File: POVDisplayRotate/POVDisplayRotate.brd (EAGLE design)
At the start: 80 x 99 mm, 34 parts, among them IC1 317EMP

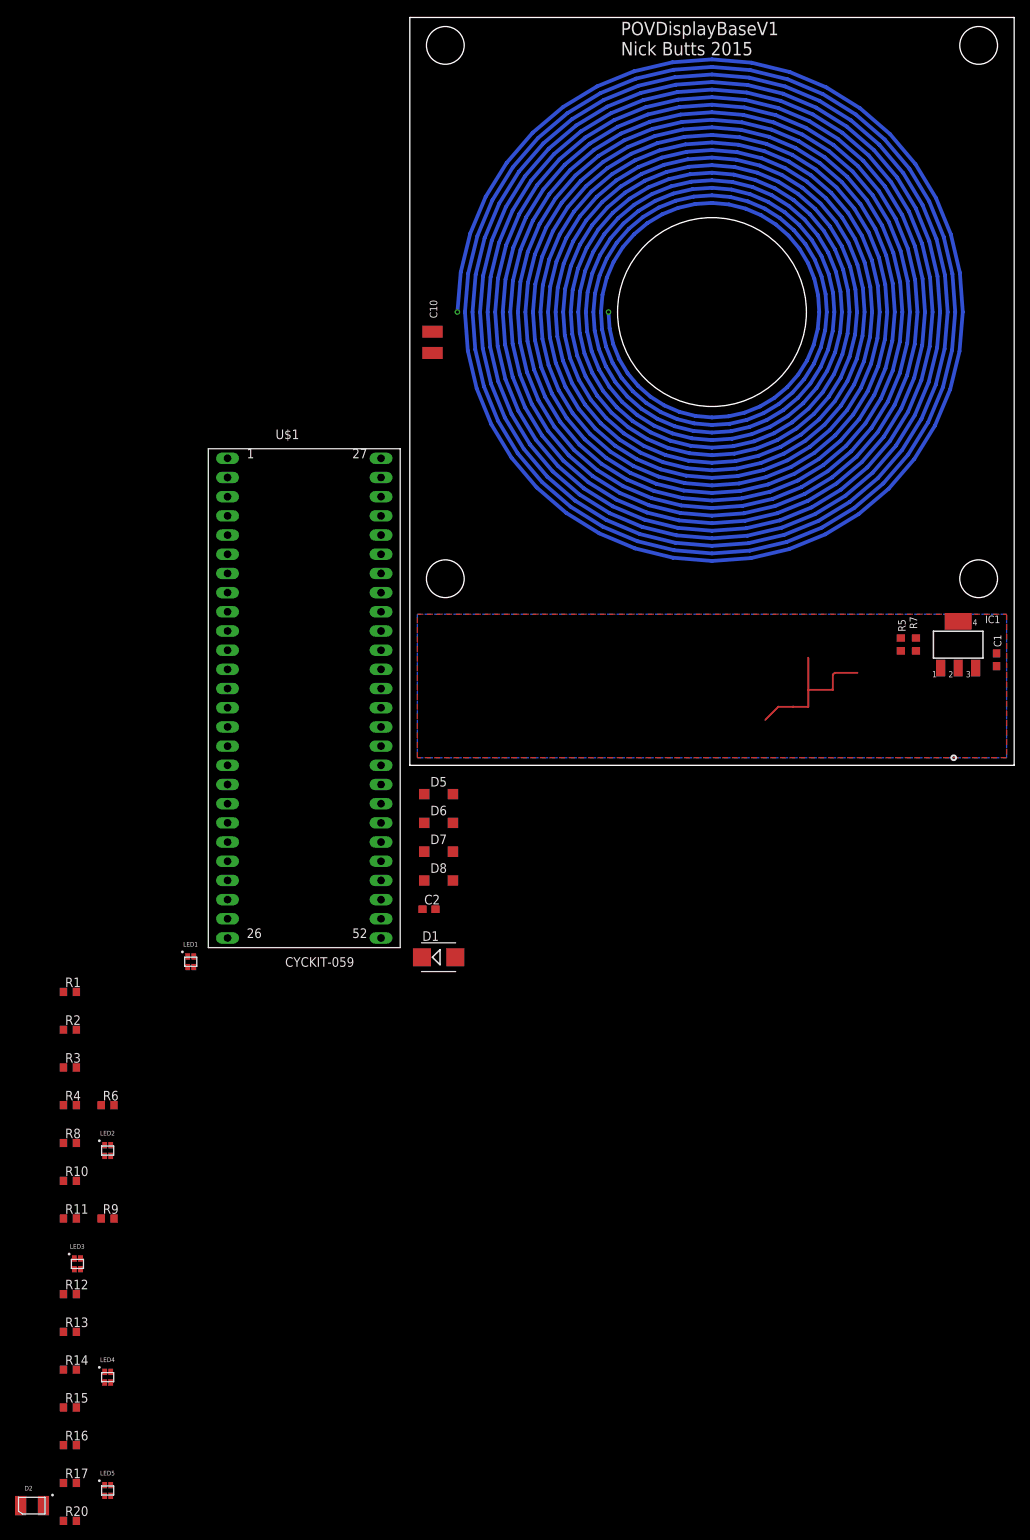
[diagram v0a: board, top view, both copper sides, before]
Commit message: Update the POVDisplayRotate.
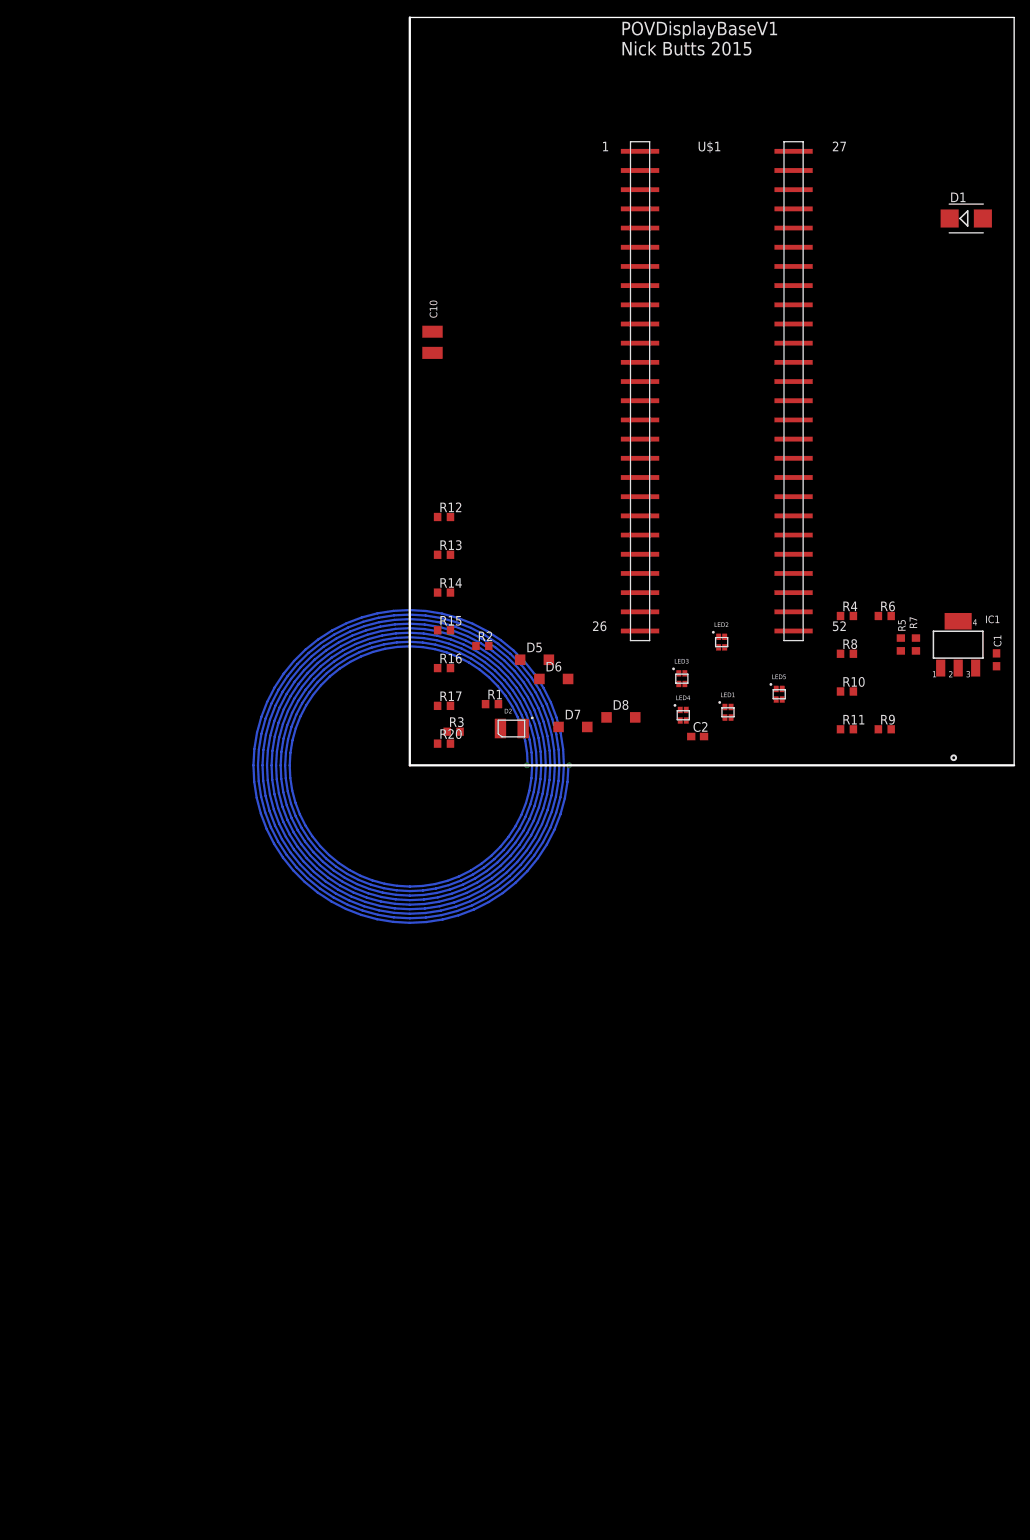
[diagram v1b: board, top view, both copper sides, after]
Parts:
- U$1: value CYCKIT-059 -> CYCKIT-059SMT; device NicksParts:CY8CKIT-059 -> NicksParts:CY8CKIT-059SM
- moved LED5 137.9 mm to (48.9, 9.41)
- moved R10 121.6 mm to (57.9, 9.77)
- moved R11 121.6 mm to (57.9, 4.77)
- moved R4 121.6 mm to (57.9, 19.8)
- moved R6 121.6 mm to (62.9, 19.8)
- moved R8 121.6 mm to (57.9, 14.8)
- moved R9 121.6 mm to (62.9, 4.77)
- moved D2 120.9 mm to (13.5, 4.87)
- moved D1 120.2 mm to (73.7, 72.4)
- moved LED4 116.1 mm to (36.2, 6.63)
- moved R12 114.2 mm to (4.53, 32.9)
- moved R13 114.2 mm to (4.53, 27.9)
- moved R14 114.2 mm to (4.53, 22.9)
- moved R15 114.2 mm to (4.53, 17.9)
- moved R16 114.2 mm to (4.53, 12.9)
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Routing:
- net N$8: track 2975.2 -> 0.00 mm, vias 2 -> 0
- net N$1: track 0.00 -> 1034.6 mm, vias 0 -> 2
- net VSS: track 21.5 -> 0.00 mm
- removed copper zone on layer 1, net GND
- removed copper zone on layer 16, net GND

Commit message: Not sure what I updated.
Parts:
- moved R11 78.5 mm to (19.0, 73.0), turned to 90 degrees
- moved R9 77.8 mm to (22.0, 71.0), turned to 270 degrees
- moved R10 76.7 mm to (16.0, 74.0), turned to 270 degrees
- moved R3 76.2 mm to (16.0, 80.0), turned to 270 degrees
- moved LED1 74.7 mm to (26.0, 80.0), turned to 90 degrees
- moved R1 71.4 mm to (19.0, 79.0), turned to 270 degrees
- moved R8 68.8 mm to (36.0, 80.0), turned to 270 degrees
- moved R6 65.4 mm to (33.0, 78.0), turned to 270 degrees
- moved LED4 65.2 mm to (26.0, 71.0), turned to 90 degrees
- moved R2 63.4 mm to (22.0, 78.0), turned to 270 degrees
- moved LED3 63.3 mm to (26.0, 74.0), turned to 90 degrees
- moved LED5 62.9 mm to (26.0, 68.0), turned to 90 degrees
- moved R4 62.8 mm to (30.0, 76.0), turned to 270 degrees
- moved LED2 62.6 mm to (26.0, 77.0), turned to 90 degrees
- moved R17 62.5 mm to (19.1, 68.7), turned to 270 degrees
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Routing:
- net N$19: track 0.00 -> 1892.7 mm, vias 0 -> 2
- net N$1: track 1034.6 -> 0.00 mm, vias 2 -> 0
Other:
- board size 80 x 99 mm -> 54 x 82 mm
- board text removed: "POVDisplayBaseV1 Nick Butts 2015"

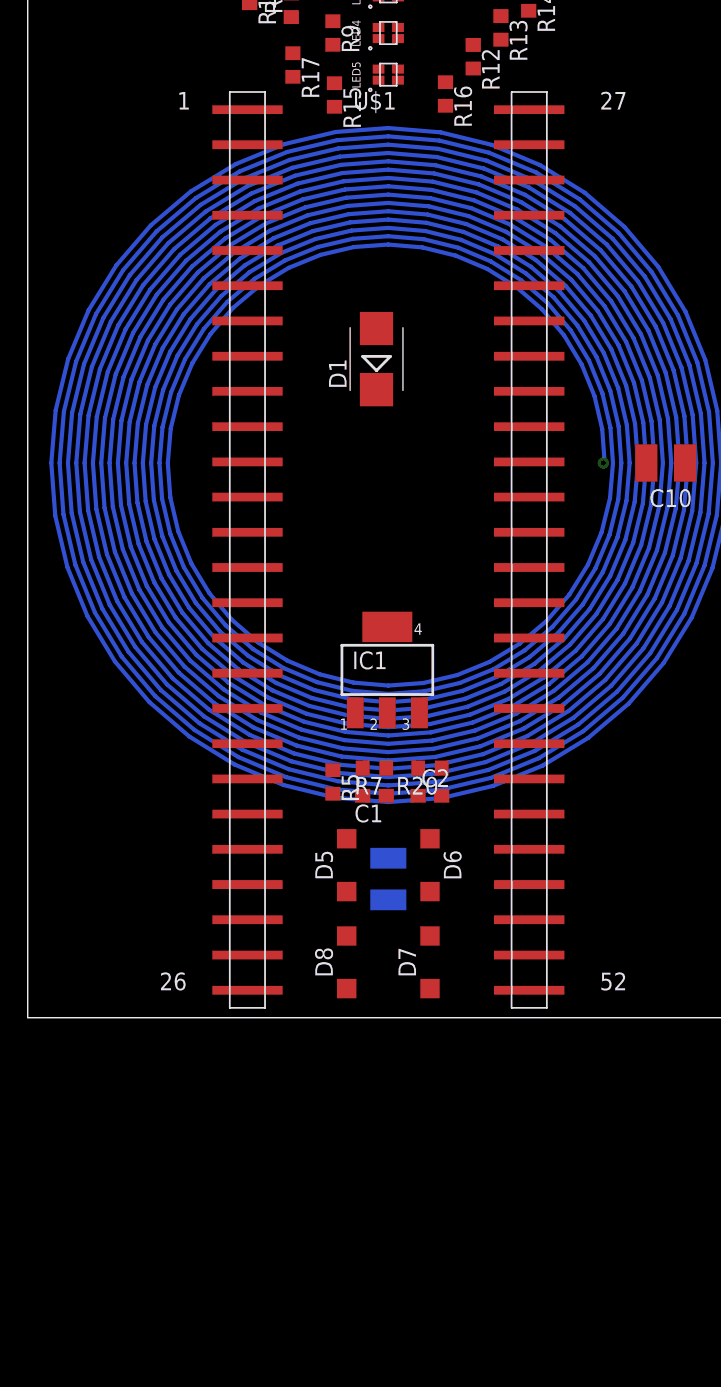
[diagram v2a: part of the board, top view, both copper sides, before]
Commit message: Added Abercrombie blockage monitor.
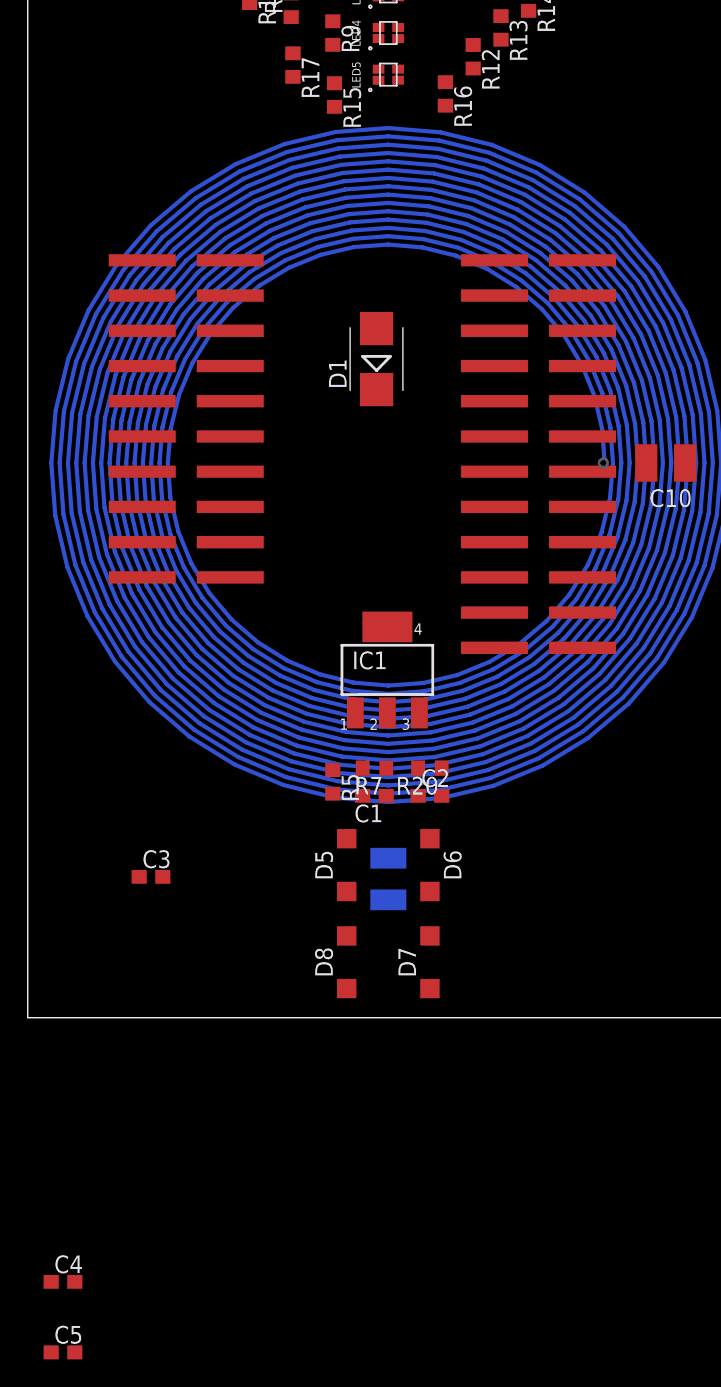
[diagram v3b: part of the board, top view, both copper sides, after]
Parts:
- removed U$1: CYCKIT-059SMT, NicksParts:CY8CKIT-059SM
- added C3: 100u, resistor:C0603
- added C4: 10u, resistor:C0603
- added C5: 1u, resistor:C0603
- added U1: CY8CKIT-142, NicksParts:CY8CKIT-142
- C10: value 2.3p -> 100n
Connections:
- new net VREF: U1.VREF
- net AGND: now also C3.2, C4.2, C5.2, U1.GND, U1.GND2; no longer U$1.25, U$1.28, U$1.52
- net BLUE1: now also U1.P3.4; no longer U$1.2
- net BLUE2: now also U1.P2.0; no longer U$1.31
- net BLUE3: now also U1.P4.0; no longer U$1.5
- net BLUE4: now also U1.P2.5; no longer U$1.35
- net BLUE5: now also U1.P2.4; no longer U$1.8
- net GREEN1: now also U1.P3.2; no longer U$1.3
- net GREEN2: now also U1.P2.1; no longer U$1.32
- net GREEN3: now also U1.P4.1; no longer U$1.6
- net GREEN4: now also U1.P2.7; no longer U$1.36
- net GREEN5: now also U1.P5.0; no longer U$1.37
- net PHOTODIODE: now also U1.P0.1; no longer U$1.34
- net RED1: now also U1.P3.6; no longer U$1.1
- net RED2: now also U1.P2.2; no longer U$1.30
- net RED3: now also U1.P3.0; no longer U$1.4
- net RED4: now also U1.P2.3; no longer U$1.33
- net RED5: now also U1.P2.6; no longer U$1.7
- net V+: no longer LED1.P$4, LED2.P$4, LED3.P$4, LED4.P$4, LED5.P$4
- net VCC: now also C3.1, C4.1, C5.1, LED1.P$4, LED2.P$4, LED3.P$4, LED4.P$4, LED5.P$4, U1.VDDA, U1.VDDD, U1.VDDR; no longer U$1.26, U$1.27

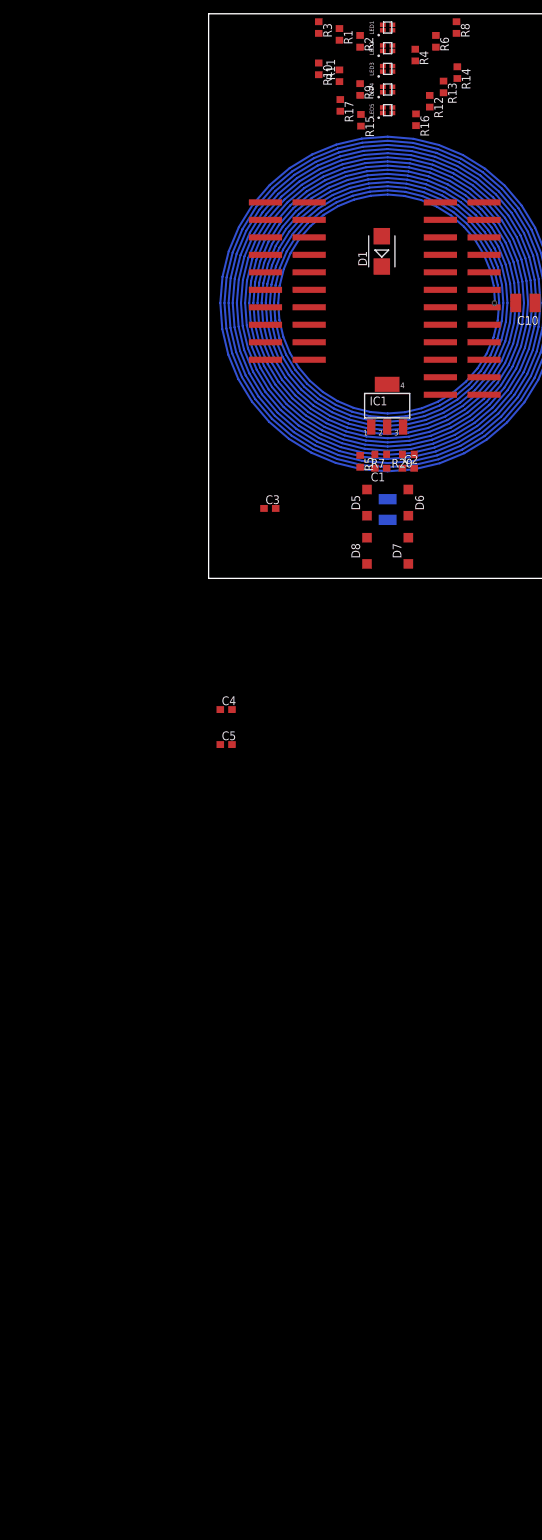
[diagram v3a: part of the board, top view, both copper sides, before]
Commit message: Updated the POVDisplayRotate
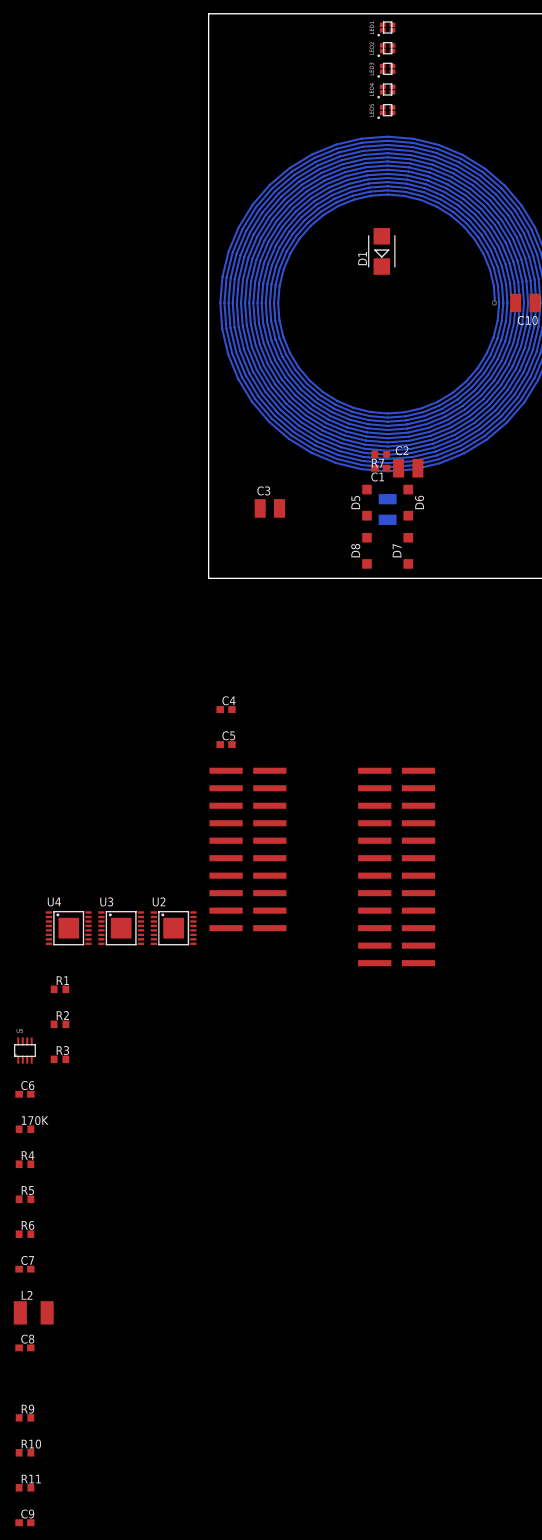
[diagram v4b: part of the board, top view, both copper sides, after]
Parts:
- removed IC1: 317EMP, linear:SOT223
- removed R12, R13, R14, R15, R16, R17, R8: 280, resistor:R0603
- removed R20: 0, resistor:R0603
- added 170K: 120, resistor:R0603
- added C6: 0.1u, resistor:C0603
- added C7: 100n, resistor:C0603
- added C8: 47u, resistor:C0603
- added C9: 5p, resistor:C0603
- added L2: 10u, resistor:L1812
- added U2, U3, U4: STP08DP05, NicksParts:SSOP16_EPAD
- added U5: MPQ4420Q, NicksParts:SOT-23-8
- C1: value 10u -> 22u
- C2: value 10u -> 1000u; device resistor:C0603 -> resistor:C1210
- C3: device resistor:C0603 -> resistor:C1210
- R1, R2, R3: value 280 -> 386
- R10, R11: value 280 -> 12k
- R4: value 280 -> 41.2k
- R5: value 200 -> 12k
- R6: value 280 -> 20
- R7: value 120 -> 51k
- R9: value 280 -> 100k
- moved R11 210.1 mm to (-26.7, -132.1), turned to 0 degrees
- moved R10 205.5 mm to (-26.7, -127.0), turned to 0 degrees
- moved R9 199.0 mm to (-26.7, -121.9), turned to 0 degrees
- moved R6 183.2 mm to (-26.7, -95.2), turned to 0 degrees
- moved R4 170.8 mm to (-26.7, -85.1), turned to 0 degrees
- moved R3 154.5 mm to (-21.6, -69.8), turned to 0 degrees
- moved R2 149.3 mm to (-21.6, -64.8), turned to 0 degrees
- moved R1 144.5 mm to (-21.6, -59.7), turned to 0 degrees
- moved R5 117.7 mm to (-26.7, -90.2), turned to 0 degrees
- moved U1 82.9 mm to (16.5, -39.4)
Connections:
- removed net BLUE1: R2.2, U1.P3.4
- removed net BLUE2: R6.2, U1.P2.0
- removed net BLUE3: R10.2, U1.P4.0
- removed net BLUE4: R13.2, U1.P2.5
- removed net BLUE5: R16.2, U1.P2.4
- removed net GREEN1: R3.2, U1.P3.2
- removed net GREEN2: R8.2, U1.P2.1
- removed net GREEN3: R11.2, U1.P4.1
- removed net GREEN4: R14.2, U1.P2.7
- removed net GREEN5: R17.2, U1.P5.0
- removed net N$13: LED4.P$1, R12.1
- removed net N$14: LED4.P$3, R13.1
- removed net N$15: LED4.P$2, R14.1
- removed net N$16: LED5.P$1, R15.1
- removed net N$17: LED5.P$3, R16.1
- removed net N$3: LED1.P$3, R2.1
- removed net PHOTODIODE: D2.P$1, U1.P0.1
- removed net RED1: R1.2, U1.P3.6
- removed net RED2: R4.2, U1.P2.2
- removed net RED3: R9.2, U1.P3.0
- removed net RED4: R12.2, U1.P2.3
- removed net RED5: R15.2, U1.P2.6
- removed net VREF: U1.VREF
- new net BLED1: LED1.BLUE, U4.5
- new net BLED2: LED2.BLUE, U4.6
- new net BLED3: LED3.BLUE, U4.7
- new net BLED4: LED4.BLUE, U4.8
- new net BLED5: LED5.BLUE, U4.9
- new net GLED1: LED1.GREEN, U3.5
- new net GLED2: LED2.GREEN, U3.6
- new net GLED3: LED3.GREEN, U3.7
- new net GLED4: LED4.GREEN, U3.8
- new net GLED5: LED5.GREEN, U3.9
- new net LE1: U2.4
- new net LE2: U3.4
- new net LE3: U4.4
- new net N$1: C6.1, U5.7
- new net N$8: C7.1, R6.1
- new net OE1: U2.13
- new net OE2: U3.13
- new net OE3: U4.13
- new net OPAMP1_NEG: C9.2, D2.P$2, R9.2
- new net OPAMP1_OUT: C9.1, R9.1
- new net OPAMP1_PLUS: R10.2, R11.1
- new net RLED1: LED1.RED, U2.5
- new net RLED2: LED2.RED, U2.6
- new net RLED3: LED3.RED, U2.7
- new net RLED4: LED4.RED, U2.8
- new net RLED5: LED5.RED, U2.9
- new net SCLK: U2.3, U3.3, U4.3
- new net SDI: U2.2
- net AGND: now also C6.2, C8.2, D2.P$1, R1.2, R11.2, R2.2, R3.2, U1.GND1, U2.1, U2.GND, U3.1, U3.GND, U4.1, U4.GND, U5.4; no longer D2.P$2
- net N$10: now also R2.1, U3.15; no longer LED3.P$1, R9.1
- net N$11: now also U3.14, U4.2; no longer LED3.P$3, R10.1
- net N$12: now also R3.1, U4.15; no longer LED3.P$2, R11.1
- net N$18: now also U2.14, U3.2; no longer LED5.P$2, R17.1
- net N$2: now also 170K.2, U5.6; no longer LED1.P$1, R1.1
- net N$4: now also R7.2, U5.8; no longer LED1.P$2, R3.1
- net N$5: now also R4.2, R5.1, R7.1; no longer LED2.P$1, R4.1
- net N$6: now also R1.1, U2.15; no longer LED2.P$3, R6.1
- net N$7: now also R6.2, U5.5; no longer IC1.1, R5.1, R7.2
- net N$9: now also C7.2, L2.1, U5.3; no longer LED2.P$2, R8.1
- net V+: now also 170K.1, U5.2; no longer IC1.3, R20.1
- net VCC: now also C8.1, L2.2, LED1.A, LED2.A, LED3.A, LED4.A, LED5.A, R10.1, R4.1, U2.16, U3.16, U4.16; no longer IC1.4, LED1.P$4, LED2.P$4, LED3.P$4, LED4.P$4, LED5.P$4, R20.2, R7.1
